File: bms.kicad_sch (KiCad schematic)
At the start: 30 parts, among them Q1 SSM6K513NU-LF, Q2 SSM6K513NU-LF, Q3 2N7002W, U1 BQ28Z620DRZR

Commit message: Placement concept is finished.
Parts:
- removed D6, D7: SM6T6V8A, Diode_SMD:D_SMB, symbol Diode:SM6T6V8A
- added D6, D7: ESD5Zxx, Diode_SMD:D_SOD-523, symbol Diode:ESD5Zxx
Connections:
- net GNDD: now also D6.2 (A), D7.2 (A)
- net comm.SCL: now also D6.1 (K)
- net comm.SDA: now also D7.1 (K)
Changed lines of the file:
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@@
+	)
+	(symbol
+		(lib_id "Diode:ESD5Zxx")
+		(at 215.9 104.14 270)
+		(unit 1)
+		(body_style 1)
+		(exclude_from_sim no)
+		(in_bom yes)
+		(on_board yes)
+		(in_pos_files yes)
+		(dnp no)
+		(fields_autoplaced yes)
+		(property "Reference" "D7"
+			(at 218.44 102.8699 90)
+			(show_name no)
+			(do_not_autoplace no)
+			(effects
+				(font
+					(size 1.27 1.27)
+				)
+				(justify left)
+			)
+		)
+		(property "Value" "ESD5Zxx"
+			(at 218.44 105.4099 90)
+			(show_name no)
+			(do_not_autoplace no)
+			(effects
+				(font
+					(size 1.27 1.27)
+				)
+				(justify left)
+			)
+		)
+		(property "Footprint" "Diode_SMD:D_SOD-523"
+			(at 211.455 104.14 0)
+			(hide yes)
+			(show_name no)
+			(do_not_autoplace no)
+			(effects
+				(font
+					(size 1.27 1.27)
+				)
+			)
+		)
+		(property "Datasheet" "https://www.onsemi.com/pdf/datasheet/esd5z2.5t1-d.pdf"
+			(at 215.9 104.14 0)
+			(hide yes)
+			(show_name no)
+			(do_not_autoplace no)
+			(effects
+				(font
+					(size 1.27 1.27)
+				)
+			)
+		)
+		(property "Description" "ESD Protection Diode, SOD-523"
+			(at 215.9 104.14 0)
+			(hide yes)
+			(show_name no)
+			(do_not_autoplace no)
+			(effects
+				(font
+					(size 1.27 1.27)
+				)
+			)
+		)
+		(pin "1"
+		)
+		(pin "2"
+		)
+		(instances
+			(project "MoistureESP"
+				(path "/f2b9f638-139e-46ec-aa60-77c4af989196/b13ba67b-4069-4f36-b5d0-6a46a6b78ce9"
+					(reference "D7")
+					(unit 1)
+				)
+			)
+		)
 	)
 	(symbol
@@
 	)
 	(symbol
-		(lib_id "Diode:SM6T6V8A")
-		(at 215.9 104.14 270)
-		(unit 1)
-		(body_style 1)
-		(exclude_from_sim no)
-		(in_bom yes)
-		(on_board yes)
-		(in_pos_files yes)
-		(dnp no)
-		(fields_autoplaced yes)
-		(property "Reference" "D7"
-			(at 218.44 102.8699 90)
-			(show_name no)
-			(do_not_autoplace no)
-			(effects
-				(font
-					(size 1.27 1.27)
-				)
-				(justify left)
-			)
-		)
-		(property "Value" "SM6T6V8A"
-			(at 218.44 105.4099 90)
-			(show_name no)
-			(do_not_autoplace no)
-			(effects
-				(font
-					(size 1.27 1.27)
-				)
-				(justify left)
-			)
-		)
-		(property "Footprint" "Diode_SMD:D_SMB"
-			(at 210.82 104.14 0)
-			(hide yes)
-			(show_name no)
-			(do_not_autoplace no)
-			(effects
-				(font
-					(size 1.27 1.27)
-				)
-			)
-		)
-		(property "Datasheet" "https://www.st.com/resource/en/datasheet/sm6t.pdf"
-			(at 215.9 102.87 0)
-			(hide yes)
-			(show_name no)
-			(do_not_autoplace no)
-			(effects
-				(font
-					(size 1.27 1.27)
-				)
-			)
-		)
-		(property "Description" "600W unidirectional Transil Transient Voltage Suppressor, 6.8Vrwm, DO-214AA"
-			(at 215.9 104.14 0)
-			(hide yes)
-			(show_name no)
-			(do_not_autoplace no)
-			(effects
-				(font
-					(size 1.27 1.27)
-				)
-			)
-		)
-		(pin "2"
-		)
-		(pin "1"
-		)
-		(instances
-			(project "MoistureESP"
-				(path "/f2b9f638-139e-46ec-aa60-77c4af989196/b13ba67b-4069-4f36-b5d0-6a46a6b78ce9"
-					(reference "D7")
-					(unit 1)
-				)
-			)
-		)
-	)
-	(symbol
 		(lib_id "power:GNDD")
 		(at 209.55 109.22 0)
@@
 	)
 	(symbol
-		(lib_id "Diode:SM6T6V8A")
-		(at 209.55 104.14 270)
-		(unit 1)
-		(body_style 1)
-		(exclude_from_sim no)
-		(in_bom yes)
-		(on_board yes)
-		(in_pos_files yes)
-		(dnp no)
-		(property "Reference" "D6"
-			(at 204.724 103.378 90)
-			(show_name no)
-			(do_not_autoplace no)
-			(effects
-				(font
-					(size 1.27 1.27)
-				)
-				(justify left)
-			)
-		)
-		(property "Value" "SM6T6V8A"
-			(at 197.358 105.664 90)
-			(show_name no)
-			(do_not_autoplace no)
-			(effects
-				(font
-					(size 1.27 1.27)
-				)
-				(justify left)
-			)
-		)
-		(property "Footprint" "Diode_SMD:D_SMB"
-			(at 204.47 104.14 0)
-			(hide yes)
-			(show_name no)
-			(do_not_autoplace no)
-			(effects
-				(font
-					(size 1.27 1.27)
-				)
-			)
-		)
-		(property "Datasheet" "https://www.st.com/resource/en/datasheet/sm6t.pdf"
-			(at 209.55 102.87 0)
-			(hide yes)
-			(show_name no)
-			(do_not_autoplace no)
-			(effects
-				(font
-					(size 1.27 1.27)
-				)
-			)
-		)
-		(property "Description" "600W unidirectional Transil Transient Voltage Suppressor, 6.8Vrwm, DO-214AA"
-			(at 209.55 104.14 0)
-			(hide yes)
-			(show_name no)
-			(do_not_autoplace no)
-			(effects
-				(font
-					(size 1.27 1.27)
-				)
-			)
-		)
-		(pin "2"
-		)
-		(pin "1"
-		)
-		(instances
-			(project "MoistureESP"
-				(path "/f2b9f638-139e-46ec-aa60-77c4af989196/b13ba67b-4069-4f36-b5d0-6a46a6b78ce9"
-					(reference "D6")
-					(unit 1)
-				)
-			)
-		)
-	)
-	(symbol
 		(lib_id "power:GND1")
 		(at 50.8 101.6 0)
@@
 					(unit 1)
 				)
+			)
+		)
+	)
+	(symbol
+		(lib_id "Diode:ESD5Zxx")
+		(at 209.55 104.14 270)
+		(unit 1)
+		(body_style 1)
+		(exclude_from_sim no)
+		(in_bom yes)
+		(on_board yes)
+		(in_pos_files yes)
+		(dnp no)
+		(fields_autoplaced yes)
+		(property "Reference" "D6"
+			(at 212.09 102.8699 90)
+			(show_name no)
+			(do_not_autoplace no)
+			(effects
+				(font
+					(size 1.27 1.27)
+				)
+				(justify left)
+			)
+		)
+		(property "Value" "ESD5Zxx"
+			(at 212.09 105.4099 90)
+			(show_name no)
+			(do_not_autoplace no)
+			(effects
+				(font
+					(size 1.27 1.27)
+				)
+				(justify left)
+			)
+		)
+		(property "Footprint" "Diode_SMD:D_SOD-523"
+			(at 205.105 104.14 0)
+			(hide yes)
+			(show_name no)
+			(do_not_autoplace no)
+			(effects
+				(font
+					(size 1.27 1.27)
+				)
+			)
+		)
+		(property "Datasheet" "https://www.onsemi.com/pdf/datasheet/esd5z2.5t1-d.pdf"
+			(at 209.55 104.14 0)
+			(hide yes)
+			(show_name no)
+			(do_not_autoplace no)
+			(effects
+				(font
+					(size 1.27 1.27)
+				)
+			)
+		)
+		(property "Description" "ESD Protection Diode, SOD-523"
+			(at 209.55 104.14 0)
+			(hide yes)
+			(show_name no)
+			(do_not_autoplace no)
+			(effects
+				(font
+					(size 1.27 1.27)
+				)
+			)
+		)
+		(pin "2"
+		)
+		(pin "1"
+		)
+		(instances
+			(project "MoistureESP"
+				(path "/f2b9f638-139e-46ec-aa60-77c4af989196/b13ba67b-4069-4f36-b5d0-6a46a6b78ce9"
+					(reference "D6")
+					(unit 1)
+				)

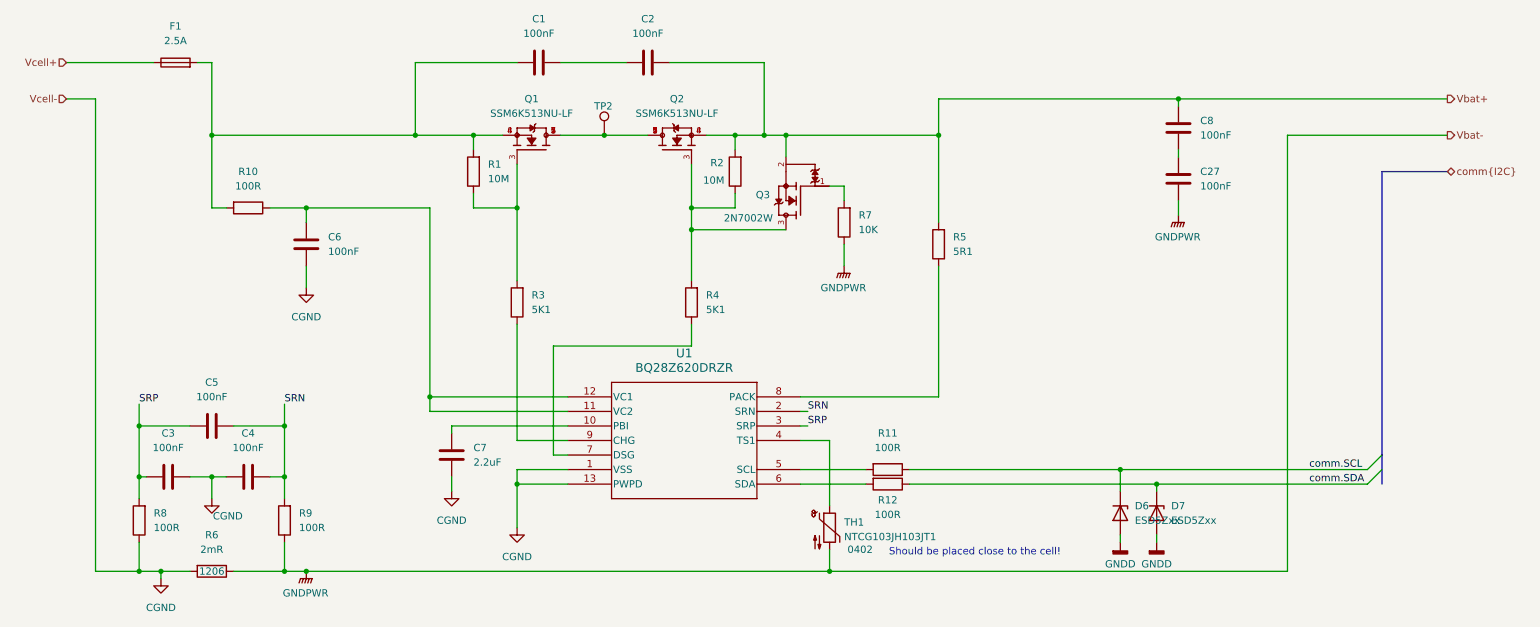
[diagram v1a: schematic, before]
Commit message: Add wiring, change footprint to avoid fatal errors at pads.
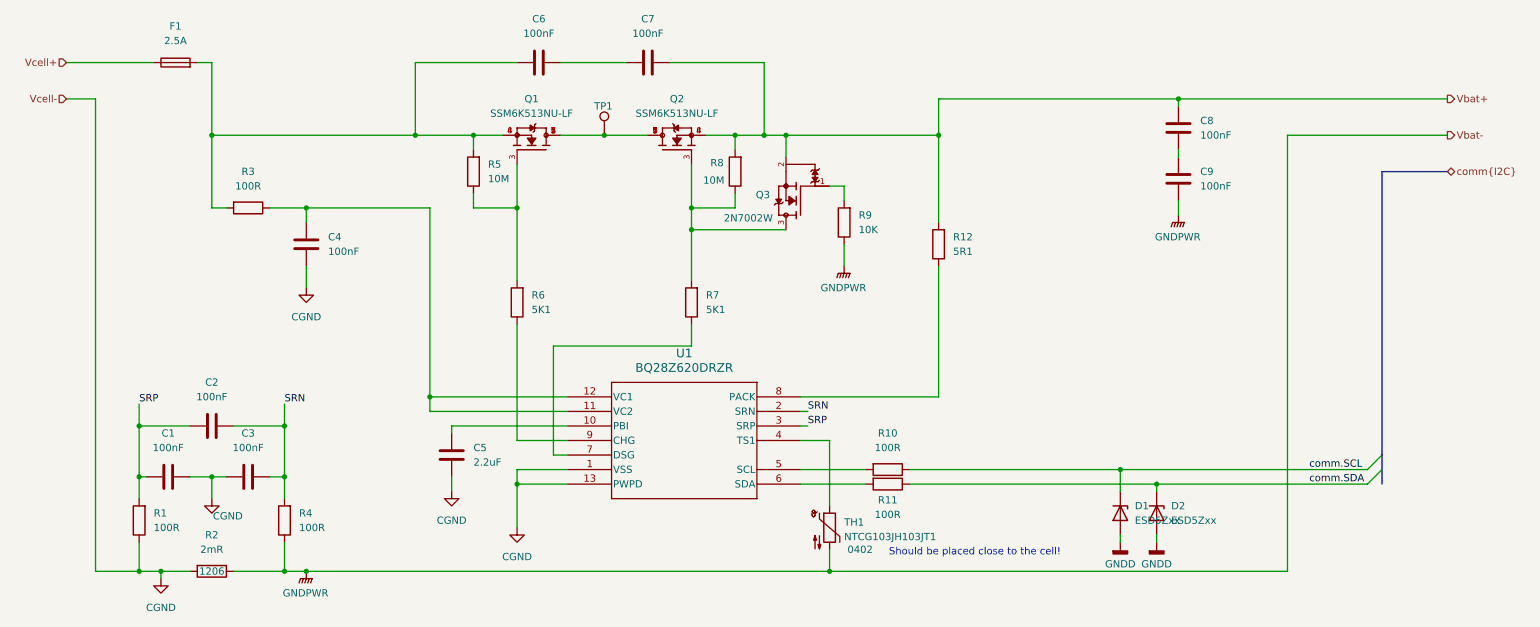
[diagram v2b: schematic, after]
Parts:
- renumbered C3 to C1, C5 to C2, C4 to C3, C6 to C4, C7 to C5, C1 to C6, C2 to C7, C27 to C9, D6 to D1, D7 to D2, R8 to R1, R11 to R10, R12 to R11, R5 to R12, R6 to R2, R10 to R3, R9 to R4, R1 to R5, R3 to R6, R4 to R7, R2 to R8, R7 to R9, TP2 to TP1

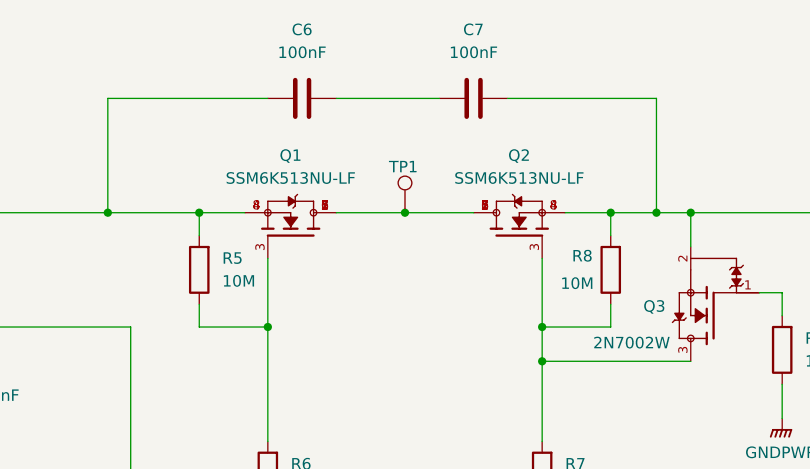
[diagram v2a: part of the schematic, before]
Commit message: Add VBAT polygon, add BQ control wiring.
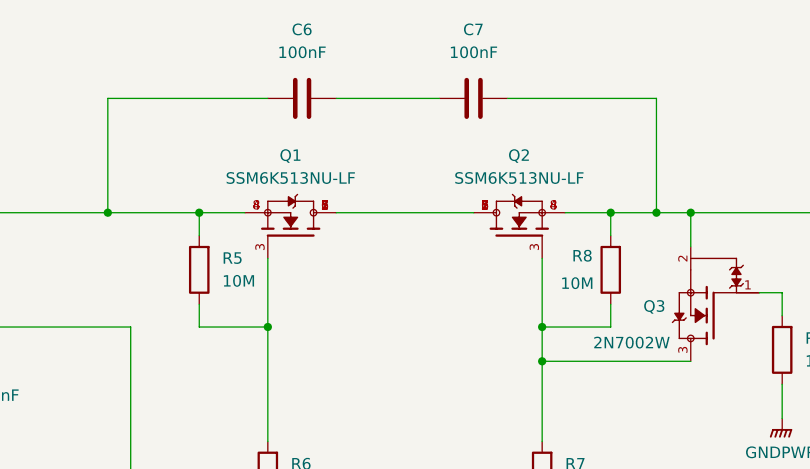
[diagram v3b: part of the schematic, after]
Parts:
- removed TP1: TestPoint, TestPoint:TestPoint_Pad_D1.5mm, symbol Connector:TestPoint
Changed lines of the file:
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@@
 	)
 	(junction
-		(at 119.38 38.1)
-		(diameter 0)
-		(color 0 0 0 0)
-	)
-	(junction
 		(at 50.8 97.79)
 		(diameter 0)
@@
 	(wire
 		(pts
-			(xy 111.76 38.1) (xy 119.38 38.1)
+			(xy 111.76 38.1) (xy 127 38.1)
 		)
 		(stroke
@@
 	(wire
 		(pts
-			(xy 119.38 38.1) (xy 127 38.1)
-		)
-		(stroke
-			(width 0)
-			(type default)
-		)
-	)
-	(wire
-		(pts
 			(xy 172.72 99.06) (xy 215.9 99.06)
 		)
@@
 					(unit 1)
 				)
-			)
-		)
-	)
-	(symbol
-		(lib_id "Connector:TestPoint")
-		(at 119.38 38.1 0)
-		(unit 1)
-		(body_style 1)
-		(exclude_from_sim no)
-		(in_bom yes)
-		(on_board yes)
-		(in_pos_files yes)
-		(dnp no)
-		(property "Reference" "TP1"
-			(at 117.602 33.02 0)
-			(show_name no)
-			(do_not_autoplace no)
-			(effects
-				(font
-					(size 1.27 1.27)
-				)
-				(justify left)
-			)
-		)
-		(property "Value" "TestPoint"
-			(at 116.078 39.878 0)
-			(hide yes)
-			(show_name no)
-			(do_not_autoplace no)
-			(effects
-				(font
-					(size 1.27 1.27)
-				)
-				(justify left)
-			)
-		)
-		(property "Footprint" "TestPoint:TestPoint_Pad_D1.5mm"
-			(at 124.46 38.1 0)
-			(hide yes)
-			(show_name no)
-			(do_not_autoplace no)
-			(effects
-				(font
-					(size 1.27 1.27)
-				)
-			)
-		)
-		(property "Datasheet" ""
-			(at 124.46 38.1 0)
-			(hide yes)
-			(show_name no)
-			(do_not_autoplace no)
-			(effects
-				(font
-					(size 1.27 1.27)
-				)
-			)
-		)
-		(property "Description" "test point"
-			(at 119.38 38.1 0)
-			(hide yes)
-			(show_name no)
-			(do_not_autoplace no)
-			(effects
-				(font
-					(size 1.27 1.27)
-				)
-			)
-		)
-		(pin "1"
-		)
-		(instances
-			(project "MoistureESP"
-				(path "/f2b9f638-139e-46ec-aa60-77c4af989196/b13ba67b-4069-4f36-b5d0-6a46a6b78ce9"
-					(reference "TP1")
-					(unit 1)
-				)

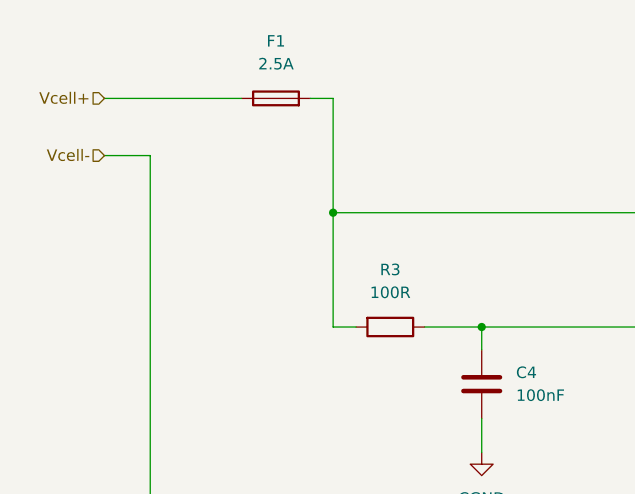
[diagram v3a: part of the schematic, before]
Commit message: Fix BQ cell voltage wrong connection.
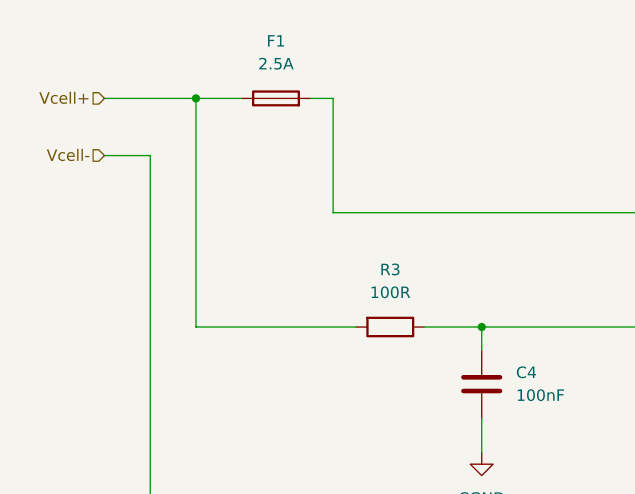
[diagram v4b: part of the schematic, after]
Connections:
- net Vcell+: now also R3.2
- net at C6.1, F1.2, Q1.4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: no longer R3.2
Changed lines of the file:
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@@
 	)
 	(junction
-		(at 50.8 38.1)
+		(at 35.56 25.4)
 		(diameter 0)
 		(color 0 0 0 0)
@@
 	(wire
 		(pts
-			(xy 50.8 38.1) (xy 50.8 50.8)
-		)
-		(stroke
-			(width 0)
-			(type default)
-		)
-	)
-	(wire
-		(pts
 			(xy 38.1 114.3) (xy 41.91 114.3)
 		)
@@
 	(wire
 		(pts
+			(xy 35.56 50.8) (xy 35.56 25.4)
+		)
+		(stroke
+			(width 0)
+			(type default)
+		)
+	)
+	(wire
+		(pts
 			(xy 50.8 97.79) (xy 50.8 101.6)
 		)
@@
 	(wire
 		(pts
-			(xy 50.8 50.8) (xy 53.34 50.8)
+			(xy 35.56 50.8) (xy 53.34 50.8)
 		)
 		(stroke
@@
 	(wire
 		(pts
-			(xy 25.4 25.4) (xy 40.64 25.4)
+			(xy 25.4 25.4) (xy 35.56 25.4)
 		)
 		(stroke
@@
 		)
 		(stroke
+			(width 0)
+			(type default)
+		)
+	)
+	(wire
+		(pts
+			(xy 35.56 25.4) (xy 40.64 25.4)
+		)
+		(stroke
